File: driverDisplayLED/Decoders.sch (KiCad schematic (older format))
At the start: 9 parts, among them J1 Conn_02x08_Counter_Clockwise, U1 74HC245, U2 74HC245, U3 74HC138D, U4 74HC138D

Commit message: Agrego codigos de catalogo, documentación, y linkeo del borrador del PCB
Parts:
- C1, C2: value C -> 1u
- R4: footprint (none) -> Resistor_SMD:R_0201_0603Metric
- RN1: value R_Network04 -> 50
- U1, U2: CodigoCatalogo (none) -> 296-1584-5-ND
- U3, U4: CodigoCatalogo (none) -> 1727-2781-2-ND - Tape & Reel (TR)
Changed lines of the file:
@@
 F 2 "Package_SO:SO-20-1EP_7.52x12.825mm_P1.27mm_EP6.045x12.09mm_Mask3.56x4.47mm" H 2500 4350 50  0001 C CNN
 F 3 "http://www.ti.com/lit/gpn/sn74HC245" H 2500 4350 50  0001 C CNN
+F 4 "296-1584-5-ND" H 2500 4350 50  0001 C CNN "CodigoCatalogo"
 	1    2500 4350
 	1    0    0    -1
@@
 F 2 "Package_SO:SO-20-1EP_7.52x12.825mm_P1.27mm_EP6.045x12.09mm_Mask3.56x4.47mm" H 5800 4500 50  0001 C CNN
 F 3 "http://www.ti.com/lit/gpn/sn74HC245" H 5800 4500 50  0001 C CNN
+F 4 "296-1584-5-ND" H 5800 4500 50  0001 C CNN "CodigoCatalogo"
 	1    5800 4500
 	1    0    0    -1
@@
 AR Path="/5FD43255/60588FA0" Ref="C1"  Part="1"
 F 0 "C1" V 2648 3395 50  0000 C CNN
-F 1 "C" V 2739 3395 50  0000 C CNN
+F 1 "1u" V 2739 3395 50  0000 C CNN
 F 2 "Capacitor_SMD:C_0201_0603Metric" H 2938 3245 50  0001 C CNN
 F 3 "~" H 2900 3395 50  0001 C CNN
@@
 F 6 "SOIC-16" H 8450 3225 50  0001 L BNN "Field6"
 F 7 "NXP" H 8450 3225 50  0001 L BNN "Field7"
+F 8 "1727-2781-2-ND - Tape & Reel (TR)" H 8450 3225 50  0001 C CNN "CodigoCatalogo"
 	1    8450 3225
 	1    0    0    -1
@@
 AR Path="/5FD43255/60588FF6" Ref="RN1"  Part="1"
 F 0 "RN1" H 2770 5129 50  0000 R CNN
-F 1 "R_Network04" V 3250 5425 50  0000 R CNN
+F 1 "50" V 3250 5425 50  0000 R CNN
 F 2 "Resistor_SMD:R_Array_Convex_4x0603" V 3325 5175 50  0001 C CNN
 F 3 "http://www.vishay.com/docs/31509/csc.pdf" H 3050 5175 50  0001 C CNN
@@
 AR Path="/5FD43255/6058903A" Ref="C2"  Part="1"
 F 0 "C2" V 5693 3510 50  0000 C CNN
-F 1 "C" V 5784 3510 50  0000 C CNN
+F 1 "1u" V 5784 3510 50  0000 C CNN
 F 2 "Capacitor_SMD:C_0201_0603Metric" H 5983 3360 50  0001 C CNN
 F 3 "~" H 5945 3510 50  0001 C CNN
@@
 F 6 "SOIC-16" H 8450 4725 50  0001 L BNN "Field6"
 F 7 "NXP" H 8450 4725 50  0001 L BNN "Field7"
+F 8 "1727-2781-2-ND - Tape & Reel (TR)" H 8450 4725 50  0001 C CNN "CodigoCatalogo"
 	1    8450 4725
 	1    0    0    -1
@@
 	1    0    0    -1
 $EndComp
-Wire Bus Line
-	9550 2725 9550 3425
-Wire Bus Line
-	9550 4200 9550 4925
 $Comp
 L Device:R R4
@@
 F 0 "R4" H 5220 3776 50  0000 L CNN
 F 1 "0" H 5220 3685 50  0000 L CNN
-F 2 "" V 5080 3730 50  0001 C CNN
+F 2 "Resistor_SMD:R_0201_0603Metric" V 5080 3730 50  0001 C CNN
 F 3 "~" H 5150 3730 50  0001 C CNN
 	1    5150 3730
@@
 Wire Wire Line
 	5150 3880 5150 4000
+Wire Bus Line
+	9550 2725 9550 3425
+Wire Bus Line
+	9550 4200 9550 4925
 $EndSCHEMATC

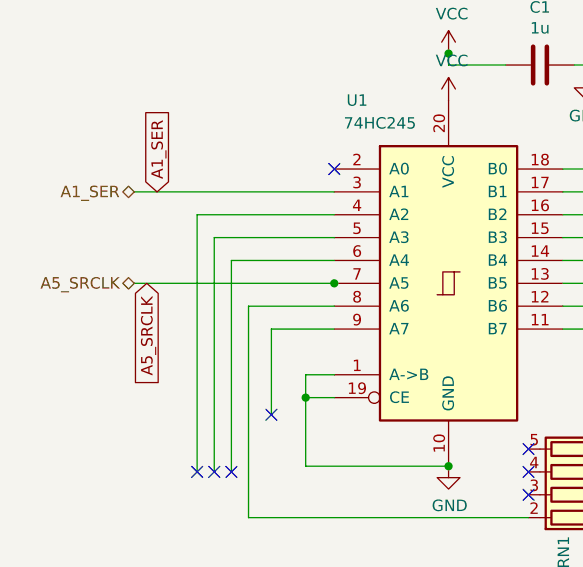
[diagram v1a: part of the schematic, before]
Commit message: corrijo conexión de pin7 U1
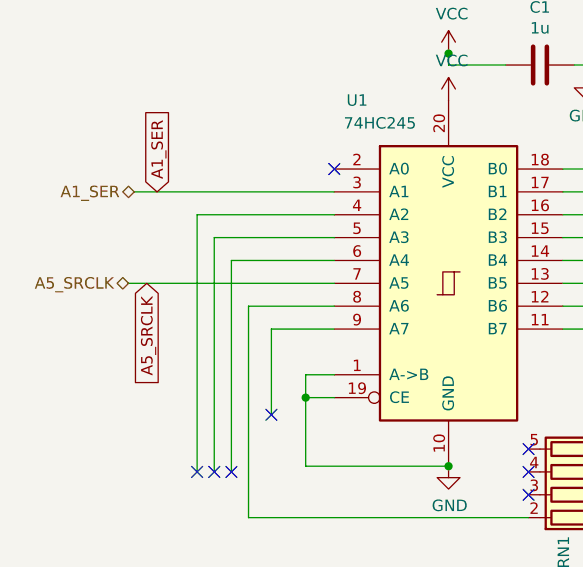
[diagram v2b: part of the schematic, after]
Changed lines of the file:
@@
 Text HLabel 1125 3950 0    50   BiDi ~ 0
 A1_SER
-Text HLabel 1125 4350 0    50   BiDi ~ 0
+Text HLabel 1100 4350 0    50   BiDi ~ 0
 A5_SRCLK
 Wire Wire Line
@@
 Text GLabel 1275 6660 2    50   Input ~ 0
 VCC
-Wire Wire Line
-	2005 4350 2000 4350
-Connection ~ 2000 4350
-Wire Wire Line
-	2000 4350 1125 4350
 Text Label 9930 4200 0    50   ~ 0
 Ya[0..7]
@@
 Wire Wire Line
 	5150 3880 5150 4000
+Wire Wire Line
+	2000 4350 1100 4350
 Wire Bus Line
 	9550 2725 9550 3425
